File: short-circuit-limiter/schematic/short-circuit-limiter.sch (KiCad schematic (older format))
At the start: 16 parts, among them P1 M1363, SW1 SWITCH_DPST, SW2 SWITCH_DPST, T1 Transformer_1P_1S, U1 DS18B20, U2 D2450, U3 D2450, U4 300XBXC1

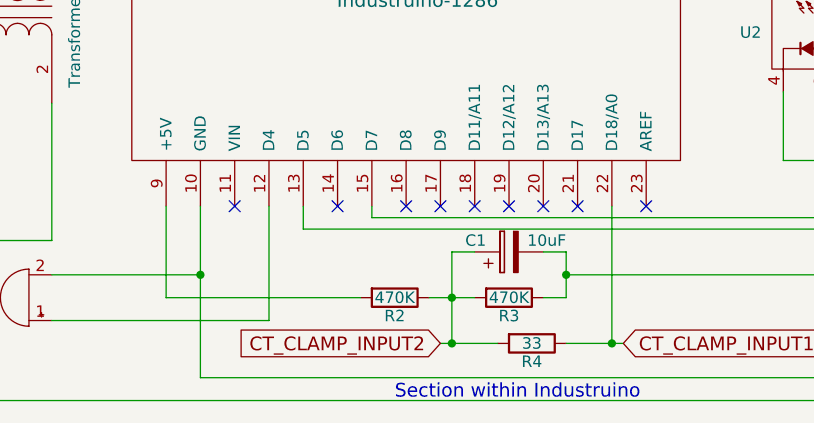
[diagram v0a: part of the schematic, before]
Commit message: update aref pin connect to 5V
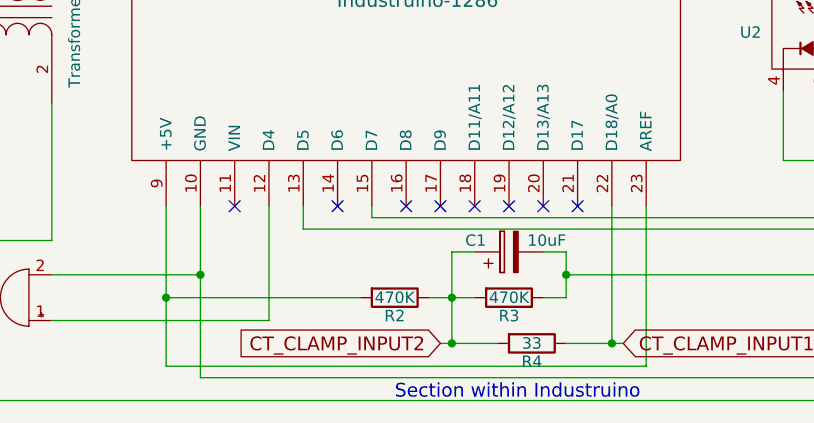
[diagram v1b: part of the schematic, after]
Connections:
- net at MCU1.23 (AREF): now also MCU1.9 (+5V), R2.2
- no-connect marks 14 -> 13
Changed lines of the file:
@@
 	4800 5250 5050 5250
 Wire Wire Line
-	3600 4650 3600 5050
+	3600 4650 3600 5350
 Wire Wire Line
 	3600 5050 4450 5050
@@
 NoConn ~ 5250 4650
 NoConn ~ 5400 4650
-NoConn ~ 5700 4650
 NoConn ~ 3900 4650
 NoConn ~ 4350 4650
@@
 NoConn ~ 3600 2950
 NoConn ~ 3750 2950
+Wire Wire Line
+	5700 4650 5700 5350
+Wire Wire Line
+	5700 5350 3600 5350
+Connection ~ 3600 5050
 $EndSCHEMATC
